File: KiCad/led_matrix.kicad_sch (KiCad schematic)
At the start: 40 parts, among them Q10 2N7002, Q11 2N7002, Q6 2N7002, Q7 2N7002, Q8 2N7002, Q9 2N7002, U10 74HC590, U11 4017, U8 74HC590, U9 74HC590

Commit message: changed more part#
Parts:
- Q10, Q11, Q6, Q7, Q8, Q9: JLCPCB Part C8545 -> C916396
- R34, R35, R36, R37, R38, R39, R40, R41, R42, R43, R44, R45, R46, R47, R48, R49, R50, R51, R52, R53, R54, R55, R56, R57: JLCPCB Part C4275 -> C112309
- R58, R59, R60, R61, R62, R63: JLCPCB Part C21190 -> C2907002
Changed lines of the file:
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@@
 			)
 		)
-		(property "JLCPCB Part" "C8545"
+		(property "JLCPCB Part" "C916396"
 			(at 153.67 142.24 0)
 			(hide yes)
@@
 			)
 		)
-		(property "JLCPCB Part" "C4275"
+		(property "JLCPCB Part" "C112309"
 			(at 53.34 39.37 90)
 			(hide yes)
@@
 			)
 		)
-		(property "JLCPCB Part" "C4275"
+		(property "JLCPCB Part" "C112309"
 			(at 52.07 86.36 90)
 			(hide yes)
@@
 			)
 		)
-		(property "JLCPCB Part" "C21190"
+		(property "JLCPCB Part" "C2907002"
 			(at 140.97 45.72 90)
 			(hide yes)
@@
 			)
 		)
-		(property "JLCPCB Part" "C4275"
+		(property "JLCPCB Part" "C112309"
 			(at 52.07 146.05 90)
 			(hide yes)
@@
 			)
 		)
-		(property "JLCPCB Part" "C4275"
+		(property "JLCPCB Part" "C112309"
 			(at 52.07 78.74 90)
 			(hide yes)
@@
 			)
 		)
-		(property "JLCPCB Part" "C4275"
+		(property "JLCPCB Part" "C112309"
 			(at 52.07 130.81 90)
 			(hide yes)
@@
 			)
 		)
-		(property "JLCPCB Part" "C21190"
+		(property "JLCPCB Part" "C2907002"
 			(at 140.97 142.24 90)
 			(hide yes)
@@
 			)
 		)
-		(property "JLCPCB Part" "C4275"
+		(property "JLCPCB Part" "C112309"
 			(at 52.07 143.51 90)
 			(hide yes)
@@
 			)
 		)
-		(property "JLCPCB Part" "C4275"
+		(property "JLCPCB Part" "C112309"
 			(at 52.07 138.43 90)
 			(hide yes)
@@
 			)
 		)
-		(property "JLCPCB Part" "C4275"
+		(property "JLCPCB Part" "C112309"
 			(at 52.07 93.98 90)
 			(hide yes)
@@
 			)
 		)
-		(property "JLCPCB Part" "C4275"
+		(property "JLCPCB Part" "C112309"
 			(at 52.07 133.35 90)
 			(hide yes)
@@
 			)
 		)
-		(property "JLCPCB Part" "C4275"
+		(property "JLCPCB Part" "C112309"
 			(at 52.07 83.82 90)
 			(hide yes)
@@
 			)
 		)
-		(property "JLCPCB Part" "C4275"
+		(property "JLCPCB Part" "C112309"
 			(at 53.34 41.91 90)
 			(hide yes)
@@
 			)
 		)
-		(property "JLCPCB Part" "C4275"
+		(property "JLCPCB Part" "C112309"
 			(at 53.34 34.29 90)
 			(hide yes)
@@
 			)
 		)
-		(property "JLCPCB Part" "C4275"
+		(property "JLCPCB Part" "C112309"
 			(at 52.07 135.89 90)
 			(hide yes)
@@
 			)
 		)
-		(property "JLCPCB Part" "C4275"
+		(property "JLCPCB Part" "C112309"
 			(at 53.34 31.75 90)
 			(hide yes)
@@
 			)
 		)
-		(property "JLCPCB Part" "C4275"
+		(property "JLCPCB Part" "C112309"
 			(at 52.07 81.28 90)
 			(hide yes)
@@
 			)
 		)
-		(property "JLCPCB Part" "C4275"
+		(property "JLCPCB Part" "C112309"
 			(at 53.34 36.83 90)
 			(hide yes)
@@
 			)
 		)
-		(property "JLCPCB Part" "C21190"
+		(property "JLCPCB Part" "C2907002"
 			(at 140.97 118.11 90)
 			(hide yes)
@@
 			)
 		)
-		(property "JLCPCB Part" "C8545"
+		(property "JLCPCB Part" "C916396"
 			(at 153.67 93.98 0)
 			(hide yes)
@@
 			)
 		)
-		(property "JLCPCB Part" "C4275"
+		(property "JLCPCB Part" "C112309"
 			(at 52.07 88.9 90)
 			(hide yes)
@@
 			)
 		)
-		(property "JLCPCB Part" "C4275"
+		(property "JLCPCB Part" "C112309"
 			(at 52.07 140.97 90)
 			(hide yes)
@@
 			)
 		)
-		(property "JLCPCB Part" "C21190"
+		(property "JLCPCB Part" "C2907002"
 			(at 140.97 69.85 90)
 			(hide yes)
@@
 			)
 		)
-		(property "JLCPCB Part" "C21190"
+		(property "JLCPCB Part" "C2907002"
 			(at 140.97 93.98 90)
 			(hide yes)
@@
 			)
 		)
-		(property "JLCPCB Part" "C4275"
+		(property "JLCPCB Part" "C112309"
 			(at 53.34 49.53 90)
 			(hide yes)
@@
 			)
 		)
-		(property "JLCPCB Part" "C8545"
+		(property "JLCPCB Part" "C916396"
 			(at 153.67 118.11 0)
 			(hide yes)
@@
 			)
 		)
-		(property "JLCPCB Part" "C4275"
+		(property "JLCPCB Part" "C112309"
 			(at 52.07 148.59 90)
 			(hide yes)
@@
 			)
 		)
-		(property "JLCPCB Part" "C8545"
+		(property "JLCPCB Part" "C916396"
 			(at 153.67 69.85 0)
 			(hide yes)
@@
 			)
 		)
-		(property "JLCPCB Part" "C8545"
+		(property "JLCPCB Part" "C916396"
 			(at 153.67 21.59 0)
 			(hide yes)
@@
 			)
 		)
-		(property "JLCPCB Part" "C4275"
+		(property "JLCPCB Part" "C112309"
 			(at 53.34 46.99 90)
 			(hide yes)
@@
 			)
 		)
-		(property "JLCPCB Part" "C4275"
+		(property "JLCPCB Part" "C112309"
 			(at 52.07 91.44 90)
 			(hide yes)
@@
 			)
 		)
-		(property "JLCPCB Part" "C21190"
+		(property "JLCPCB Part" "C2907002"
 			(at 140.97 21.59 90)
 			(hide yes)
@@
 			)
 		)
-		(property "JLCPCB Part" "C8545"
+		(property "JLCPCB Part" "C916396"
 			(at 153.67 45.72 0)
 			(hide yes)
@@
 			)
 		)
-		(property "JLCPCB Part" "C4275"
+		(property "JLCPCB Part" "C112309"
 			(at 53.34 44.45 90)
 			(hide yes)
@@
 			)
 		)
-		(property "JLCPCB Part" "C4275"
+		(property "JLCPCB Part" "C112309"
 			(at 52.07 96.52 90)
 			(hide yes)

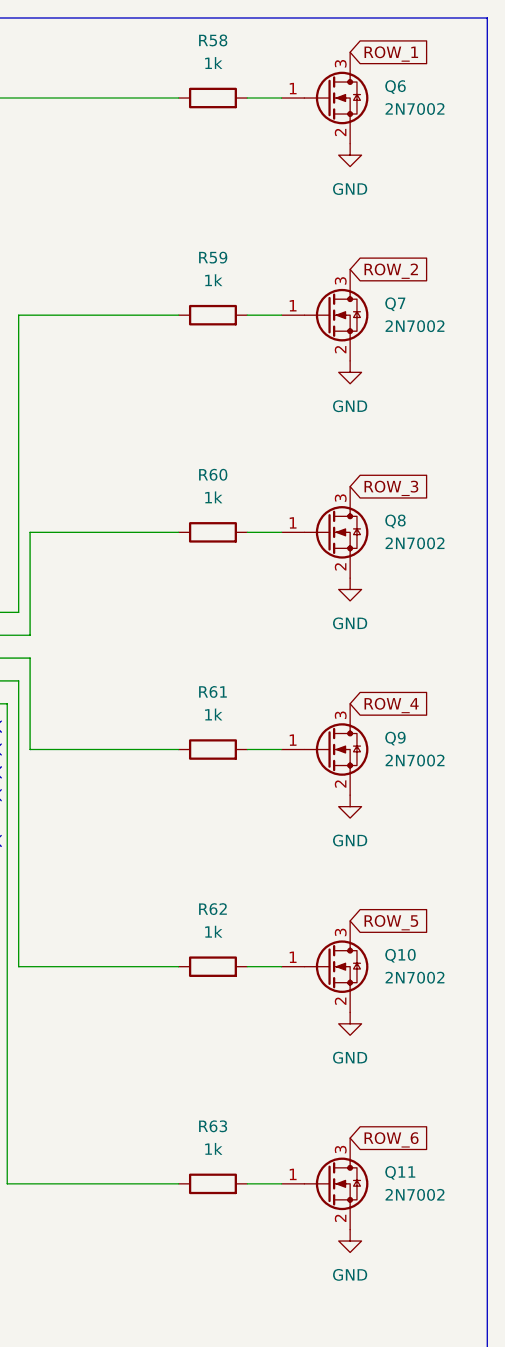
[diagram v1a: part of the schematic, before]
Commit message: changed some out of stock parts
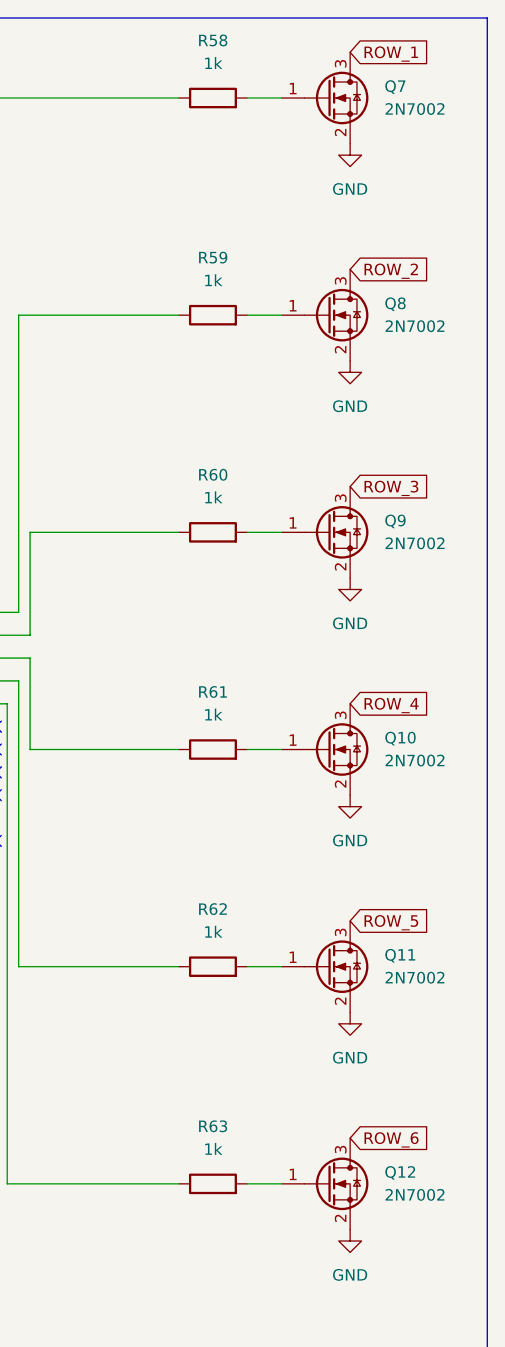
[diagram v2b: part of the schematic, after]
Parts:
- renumbered Q9 to Q10, Q10 to Q11, Q11 to Q12, Q6 to Q7, Q7 to Q8, Q8 to Q9
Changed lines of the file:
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@@
 		(dnp no)
 		(fields_autoplaced yes)
-		(property "Reference" "#PWR072"
+		(property "Reference" "#PWR073"
 			(at 38.1 165.1 0)
 			(hide yes)
@@
 			(project "Esmog_snuffelaar"
 				(path "/bcffc34a-d831-4e24-b8c4-0d923c3d51e5/8f582b23-49f5-40c4-b894-4e132e0d63cc"
-					(reference "#PWR072")
+					(reference "#PWR073")
 					(unit 1)
 				)
@@
 		(dnp no)
 		(fields_autoplaced yes)
-		(property "Reference" "Q11"
+		(property "Reference" "Q12"
 			(at 160.02 140.9699 0)
 			(show_name no)
@@
 			(project "Esmog_snuffelaar"
 				(path "/bcffc34a-d831-4e24-b8c4-0d923c3d51e5/8f582b23-49f5-40c4-b894-4e132e0d63cc"
-					(reference "Q11")
+					(reference "Q12")
 					(unit 1)
 				)
@@
 		(dnp no)
 		(fields_autoplaced yes)
-		(property "Reference" "#PWR079"
+		(property "Reference" "#PWR080"
 			(at 156.21 129.54 0)
 			(hide yes)
@@
 			(project "Esmog_snuffelaar"
 				(path "/bcffc34a-d831-4e24-b8c4-0d923c3d51e5/8f582b23-49f5-40c4-b894-4e132e0d63cc"
-					(reference "#PWR079")
+					(reference "#PWR080")
 					(unit 1)
 				)
@@
 		(dnp no)
 		(fields_autoplaced yes)
-		(property "Reference" "#PWR071"
+		(property "Reference" "#PWR072"
 			(at 38.1 129.54 0)
 			(hide yes)
@@
 			(project "Esmog_snuffelaar"
 				(path "/bcffc34a-d831-4e24-b8c4-0d923c3d51e5/8f582b23-49f5-40c4-b894-4e132e0d63cc"
-					(reference "#PWR071")
+					(reference "#PWR072")
 					(unit 1)
 				)
@@
 		(dnp no)
 		(fields_autoplaced yes)
-		(property "Reference" "#PWR074"
+		(property "Reference" "#PWR075"
 			(at 104.14 118.11 0)
 			(hide yes)
@@
 			(project "Esmog_snuffelaar"
 				(path "/bcffc34a-d831-4e24-b8c4-0d923c3d51e5/8f582b23-49f5-40c4-b894-4e132e0d63cc"
-					(reference "#PWR074")
+					(reference "#PWR075")
 					(unit 1)
 				)
@@
 		(dnp no)
 		(fields_autoplaced yes)
-		(property "Reference" "#PWR063"
+		(property "Reference" "#PWR064"
 			(at 21.59 86.36 0)
 			(hide yes)
@@
 			(project "Esmog_snuffelaar"
 				(path "/bcffc34a-d831-4e24-b8c4-0d923c3d51e5/8f582b23-49f5-40c4-b894-4e132e0d63cc"
-					(reference "#PWR063")
+					(reference "#PWR064")
 					(unit 1)
 				)
@@
 		(dnp no)
 		(fields_autoplaced yes)
-		(property "Reference" "#PWR080"
+		(property "Reference" "#PWR081"
 			(at 156.21 153.67 0)
 			(hide yes)
@@
 			(project "Esmog_snuffelaar"
 				(path "/bcffc34a-d831-4e24-b8c4-0d923c3d51e5/8f582b23-49f5-40c4-b894-4e132e0d63cc"
-					(reference "#PWR080")
+					(reference "#PWR081")
 					(unit 1)
 				)
@@
 		(dnp no)
 		(fields_autoplaced yes)
-		(property "Reference" "#PWR062"
+		(property "Reference" "#PWR063"
 			(at 31.75 44.45 0)
 			(hide yes)
@@
 			(project "Esmog_snuffelaar"
 				(path "/bcffc34a-d831-4e24-b8c4-0d923c3d51e5/8f582b23-49f5-40c4-b894-4e132e0d63cc"
-					(reference "#PWR062")
+					(reference "#PWR063")
 					(unit 1)
 				)
@@
 		(dnp no)
 		(fields_autoplaced yes)
-		(property "Reference" "#PWR069"
+		(property "Reference" "#PWR070"
 			(at 38.1 77.47 0)
 			(hide yes)
@@
 			(project "Esmog_snuffelaar"
 				(path "/bcffc34a-d831-4e24-b8c4-0d923c3d51e5/8f582b23-49f5-40c4-b894-4e132e0d63cc"
-					(reference "#PWR069")
+					(reference "#PWR070")
 					(unit 1)
 				)
@@
 		(dnp no)
 		(fields_autoplaced yes)
-		(property "Reference" "#PWR078"
+		(property "Reference" "#PWR079"
 			(at 156.21 105.41 0)
 			(hide yes)
@@
 			(project "Esmog_snuffelaar"
 				(path "/bcffc34a-d831-4e24-b8c4-0d923c3d51e5/8f582b23-49f5-40c4-b894-4e132e0d63cc"
-					(reference "#PWR078")
+					(reference "#PWR079")
 					(unit 1)
 				)
@@
 		(dnp no)
 		(fields_autoplaced yes)
-		(property "Reference" "#PWR061"
+		(property "Reference" "#PWR062"
 			(at 21.59 39.37 0)
 			(hide yes)
@@
 			(project "Esmog_snuffelaar"
 				(path "/bcffc34a-d831-4e24-b8c4-0d923c3d51e5/8f582b23-49f5-40c4-b894-4e132e0d63cc"
-					(reference "#PWR061")
+					(reference "#PWR062")
 					(unit 1)
 				)
@@
 		(dnp no)
 		(fields_autoplaced yes)
-		(property "Reference" "#PWR077"
+		(property "Reference" "#PWR078"
 			(at 156.21 81.28 0)
 			(hide yes)
@@
 			(project "Esmog_snuffelaar"
 				(path "/bcffc34a-d831-4e24-b8c4-0d923c3d51e5/8f582b23-49f5-40c4-b894-4e132e0d63cc"
-					(reference "#PWR077")
+					(reference "#PWR078")
 					(unit 1)
 				)
@@
 		(dnp no)
 		(fields_autoplaced yes)
-		(property "Reference" "#PWR068"
+		(property "Reference" "#PWR069"
 			(at 38.1 66.04 0)
 			(hide yes)
@@
 			(project "Esmog_snuffelaar"
 				(path "/bcffc34a-d831-4e24-b8c4-0d923c3d51e5/8f582b23-49f5-40c4-b894-4e132e0d63cc"
-					(reference "#PWR068")
+					(reference "#PWR069")
 					(unit 1)
 				)
@@
 		(dnp no)
 		(fields_autoplaced yes)
-		(property "Reference" "#PWR076"
+		(property "Reference" "#PWR077"
 			(at 156.21 57.15 0)
 			(hide yes)
@@
 			(project "Esmog_snuffelaar"
 				(path "/bcffc34a-d831-4e24-b8c4-0d923c3d51e5/8f582b23-49f5-40c4-b894-4e132e0d63cc"
-					(reference "#PWR076")
+					(reference "#PWR077")
 					(unit 1)
 				)
@@
 		(dnp no)
 		(fields_autoplaced yes)
-		(property "Reference" "#PWR075"
+		(property "Reference" "#PWR076"
 			(at 156.21 33.02 0)
 			(hide yes)
@@
 			(project "Esmog_snuffelaar"
 				(path "/bcffc34a-d831-4e24-b8c4-0d923c3d51e5/8f582b23-49f5-40c4-b894-4e132e0d63cc"
-					(reference "#PWR075")
+					(reference "#PWR076")
 					(unit 1)
 				)
@@
 		(dnp no)
 		(fields_autoplaced yes)
-		(property "Reference" "#PWR067"
+		(property "Reference" "#PWR068"
 			(at 38.1 30.48 0)
 			(hide yes)
@@
 			(project "Esmog_snuffelaar"
 				(path "/bcffc34a-d831-4e24-b8c4-0d923c3d51e5/8f582b23-49f5-40c4-b894-4e132e0d63cc"
-					(reference "#PWR067")
+					(reference "#PWR068")
 					(unit 1)
 				)
@@
 		(dnp no)
 		(fields_autoplaced yes)
-		(property "Reference" "#PWR070"
+		(property "Reference" "#PWR071"
 			(at 38.1 113.03 0)
 			(hide yes)
@@
 			(project "Esmog_snuffelaar"
 				(path "/bcffc34a-d831-4e24-b8c4-0d923c3d51e5/8f582b23-49f5-40c4-b894-4e132e0d63cc"
-					(reference "#PWR070")
+					(reference "#PWR071")
 					(unit 1)
 				)
@@
 		(dnp no)
 		(fields_autoplaced yes)
-		(property "Reference" "#PWR064"
+		(property "Reference" "#PWR065"
 			(at 31.75 91.44 0)
 			(hide yes)
@@
 			(project "Esmog_snuffelaar"
 				(path "/bcffc34a-d831-4e24-b8c4-0d923c3d51e5/8f582b23-49f5-40c4-b894-4e132e0d63cc"
-					(reference "#PWR064")
+					(reference "#PWR065")
 					(unit 1)
 				)
@@
 		(dnp no)
 		(fields_autoplaced yes)
-		(property "Reference" "Q9"
+		(property "Reference" "Q10"
 			(at 160.02 92.7099 0)
 			(show_name no)
@@
 			(project "Esmog_snuffelaar"
 				(path "/bcffc34a-d831-4e24-b8c4-0d923c3d51e5/8f582b23-49f5-40c4-b894-4e132e0d63cc"
-					(reference "Q9")
+					(reference "Q10")
 					(unit 1)
 				)
@@
 		(dnp no)
 		(fields_autoplaced yes)
-		(property "Reference" "#PWR073"
+		(property "Reference" "#PWR074"
 			(at 104.14 72.39 0)
 			(hide yes)
@@
 			(project "Esmog_snuffelaar"
 				(path "/bcffc34a-d831-4e24-b8c4-0d923c3d51e5/8f582b23-49f5-40c4-b894-4e132e0d63cc"
-					(reference "#PWR073")
+					(reference "#PWR074")
 					(unit 1)
 				)
@@
 		(dnp no)
 		(fields_autoplaced yes)
-		(property "Reference" "#PWR065"
+		(property "Reference" "#PWR066"
 			(at 21.59 138.43 0)
 			(hide yes)
@@
 			(project "Esmog_snuffelaar"
 				(path "/bcffc34a-d831-4e24-b8c4-0d923c3d51e5/8f582b23-49f5-40c4-b894-4e132e0d63cc"
-					(reference "#PWR065")
+					(reference "#PWR066")
 					(unit 1)
 				)
@@
 		(dnp no)
 		(fields_autoplaced yes)
-		(property "Reference" "Q10"
+		(property "Reference" "Q11"
 			(at 160.02 116.8399 0)
 			(show_name no)
@@
 			(project "Esmog_snuffelaar"
 				(path "/bcffc34a-d831-4e24-b8c4-0d923c3d51e5/8f582b23-49f5-40c4-b894-4e132e0d63cc"
-					(reference "Q10")
+					(reference "Q11")
 					(unit 1)
 				)
@@
 		(dnp no)
 		(fields_autoplaced yes)
-		(property "Reference" "Q8"
+		(property "Reference" "Q9"
 			(at 160.02 68.5799 0)
 			(show_name no)
@@
 			(project "Esmog_snuffelaar"
 				(path "/bcffc34a-d831-4e24-b8c4-0d923c3d51e5/8f582b23-49f5-40c4-b894-4e132e0d63cc"
-					(reference "Q8")
+					(reference "Q9")
 					(unit 1)
 				)
@@
 		(dnp no)
 		(fields_autoplaced yes)
-		(property "Reference" "Q6"
+		(property "Reference" "Q7"
 			(at 160.02 20.3199 0)
 			(show_name no)
@@
 			(project "Esmog_snuffelaar"
 				(path "/bcffc34a-d831-4e24-b8c4-0d923c3d51e5/8f582b23-49f5-40c4-b894-4e132e0d63cc"
-					(reference "Q6")
+					(reference "Q7")
 					(unit 1)
 				)
@@
 		(dnp no)
 		(fields_autoplaced yes)
-		(property "Reference" "Q7"
+		(property "Reference" "Q8"
 			(at 160.02 44.4499 0)
 			(show_name no)
@@
 			(project "Esmog_snuffelaar"
 				(path "/bcffc34a-d831-4e24-b8c4-0d923c3d51e5/8f582b23-49f5-40c4-b894-4e132e0d63cc"
-					(reference "Q7")
+					(reference "Q8")
 					(unit 1)
 				)
@@
 		(dnp no)
 		(fields_autoplaced yes)
-		(property "Reference" "#PWR066"
+		(property "Reference" "#PWR067"
 			(at 31.75 143.51 0)
 			(hide yes)
@@
 			(project "Esmog_snuffelaar"
 				(path "/bcffc34a-d831-4e24-b8c4-0d923c3d51e5/8f582b23-49f5-40c4-b894-4e132e0d63cc"
-					(reference "#PWR066")
+					(reference "#PWR067")
 					(unit 1)
 				)
